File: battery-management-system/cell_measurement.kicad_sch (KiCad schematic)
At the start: 21 parts, among them Q10 BS250FTA, Q11 BS250FTA, Q12 BS250FTA, Q13 BS250FTA, Q9 DMN3404L, U12 LM2904M8-13, U14 LM2904M8-13

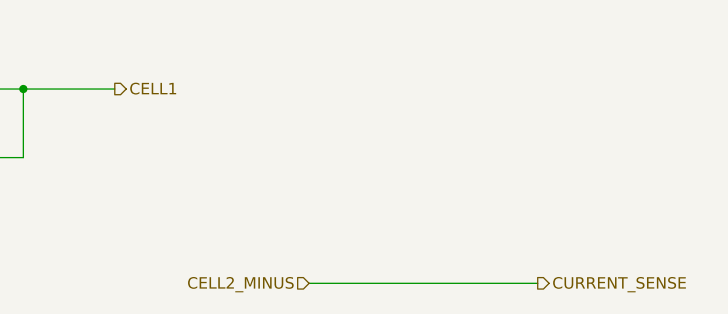
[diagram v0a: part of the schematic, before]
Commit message: fix electrical rule check errors
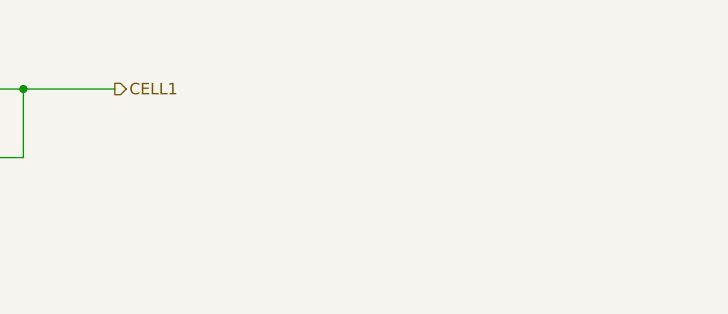
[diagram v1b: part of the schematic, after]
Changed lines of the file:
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@@
-    (stroke (width 0) (type default))
-  )
-  (wire (pts (xy 220.98 149.86) (xy 246.38 149.86))
     (stroke (width 0) (type default))
   )
@@
     (effects (font (size 1.27 1.27)) (justify left))
   )
-  (hierarchical_label "CURRENT_SENSE" (shape output) (at 246.38 149.86 0) (fields_autoplaced)
-    (effects (font (size 1.27 1.27)) (justify left))
-  )
   (hierarchical_label "CELL3" (shape output) (at 199.39 90.17 0) (fields_autoplaced)
     (effects (font (size 1.27 1.27)) (justify left))
   )
-  (hierarchical_label "CELL2_MINUS" (shape input) (at 220.98 149.86 180) (fields_autoplaced)
-    (effects (font (size 1.27 1.27)) (justify right))
-  )
   (hierarchical_label "5V" (shape input) (at 21.59 20.32 180) (fields_autoplaced)

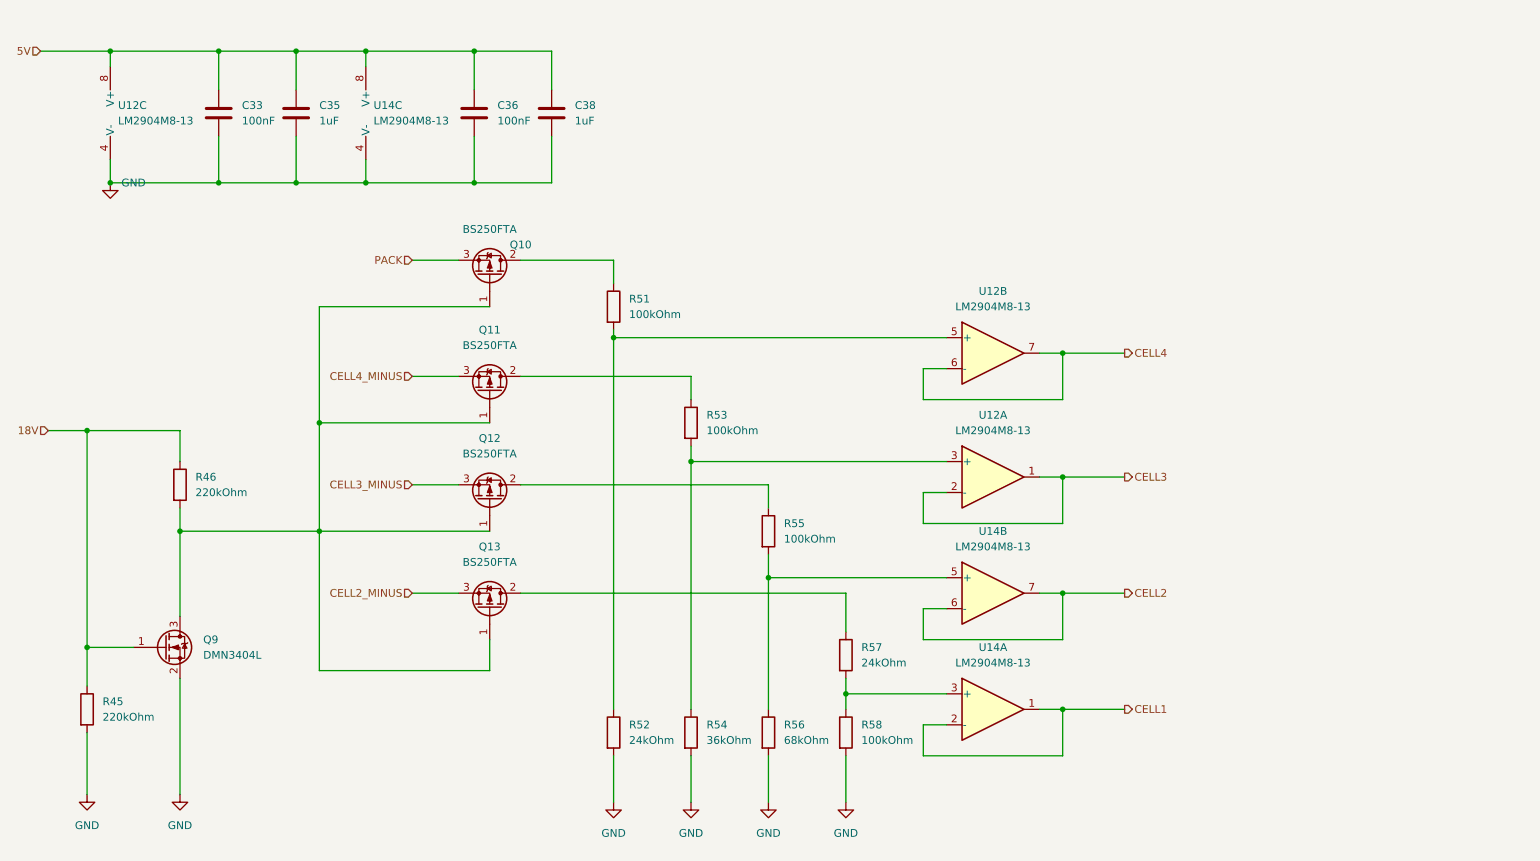
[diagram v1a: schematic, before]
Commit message: add enable input for cell measurement
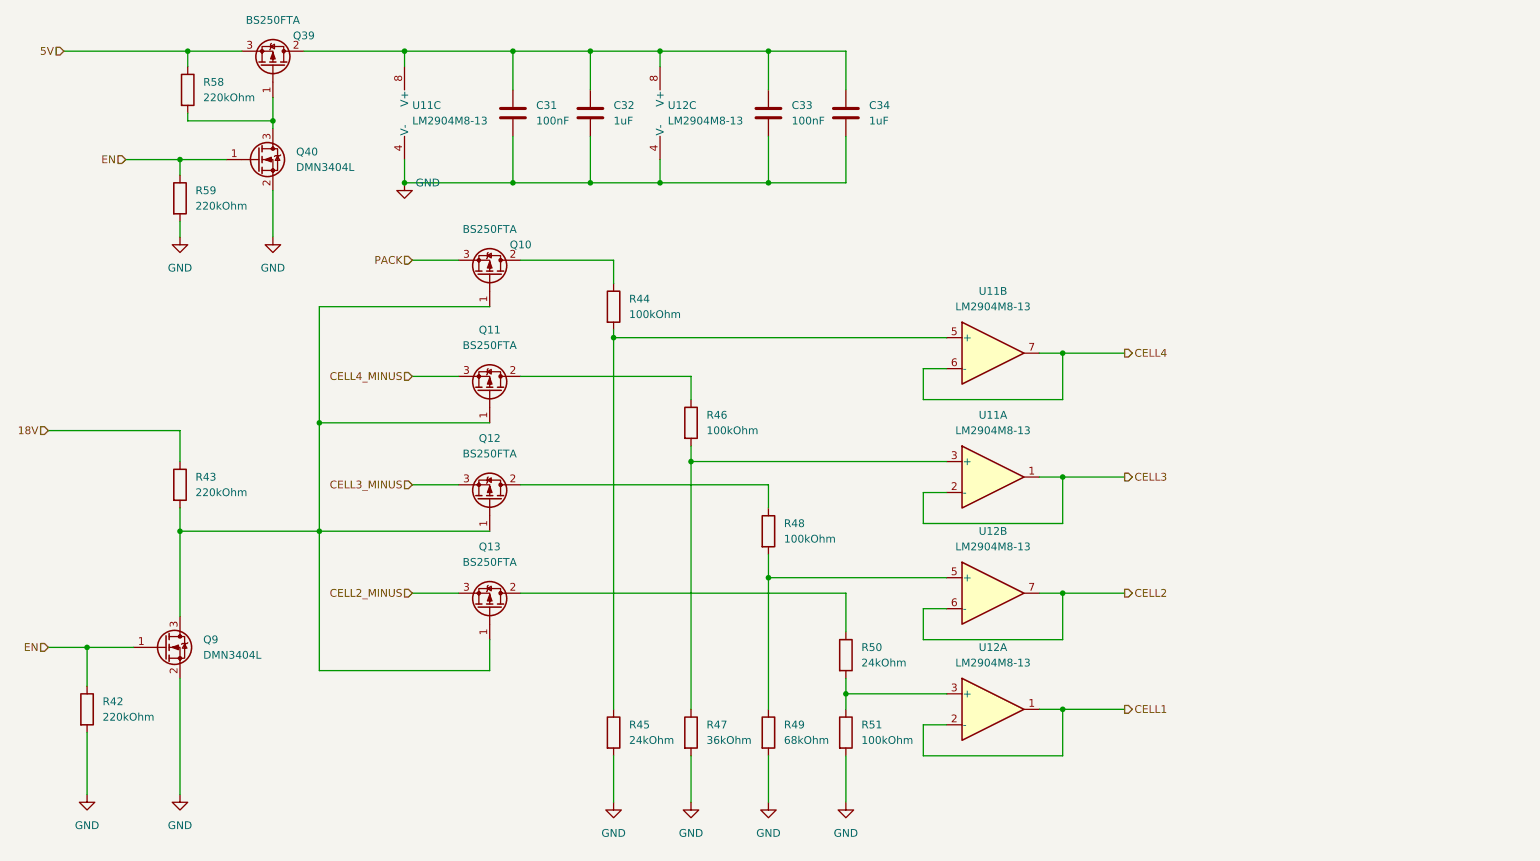
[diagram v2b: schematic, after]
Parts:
- added Q39: BS250FTA, benediktibk:SOT-23, symbol benediktibk:BS250FTA
- added Q40: DMN3404L, benediktibk:SOT-23, symbol benediktibk:DMN3404L
- added R58, R59: 220kOhm, benediktibk:R_0603_1608Metric_Pad0.98x0.95mm_HandSolder, symbol benediktibk:R_220kOhm_SMD_0603_100mW_1%
- renumbered C33 to C31, C35 to C32, C36 to C33, C38 to C34, R45 to R42, R46 to R43, R51 to R44, R52 to R45, R53 to R46, R54 to R47, R55 to R48, R56 to R49, R57 to R50, R58 to R51, U12 to U11, U14 to U12
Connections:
- net 18V: no longer Q9.1 (G), R42.1
- net 5V: now also Q39.3 (S), R58.1; no longer C31.1, C32.1, C33.1, C34.1, U11.8 (V+), U12.8 (V+)
- net GND: now also Q40.2 (S), R59.2
- new net: C31.1, C32.1, C33.1, C34.1, Q39.2 (D), U11.8 (V+), U12.8 (V+)
- new net: Q39.1 (G), Q40.3 (D), R58.2
- new net EN: Q40.1 (G), Q9.1 (G), R42.1, R59.1
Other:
- moved on the sheet: C31, C32, C33, C34, U11C, U12C

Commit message: make layout easier for cell measurement
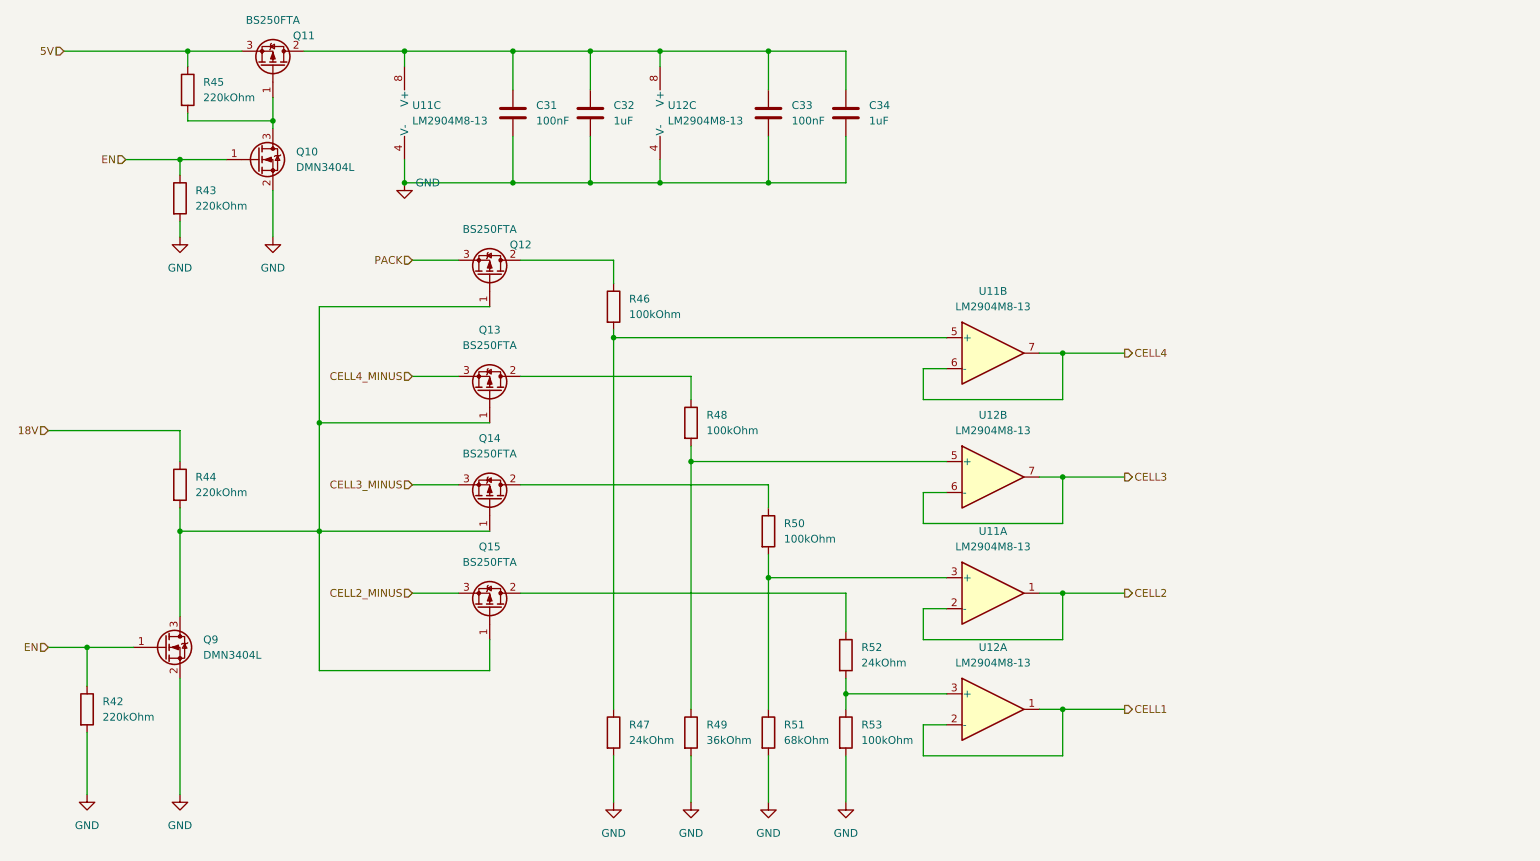
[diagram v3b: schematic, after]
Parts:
- renumbered Q40 to Q10, Q39 to Q11, Q10 to Q12, Q11 to Q13, Q12 to Q14, Q13 to Q15, R59 to R43, R43 to R44, R58 to R45, R44 to R46, R45 to R47, R46 to R48, R47 to R49, R48 to R50, R49 to R51, R50 to R52, R51 to R53
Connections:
- net CELL2: now also U11.1, U11.2 (-); no longer U12.6 (-), U12.7
- net CELL3: now also U12.6 (-), U12.7; no longer U11.1, U11.2 (-)
- net at R48.2, R49.1: now also U12.5 (+); no longer U11.3 (+)
- net at R50.2, R51.1: now also U11.3 (+); no longer U12.5 (+)
